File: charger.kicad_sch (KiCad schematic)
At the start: 6 parts, among them U1 BQ24074RGTR

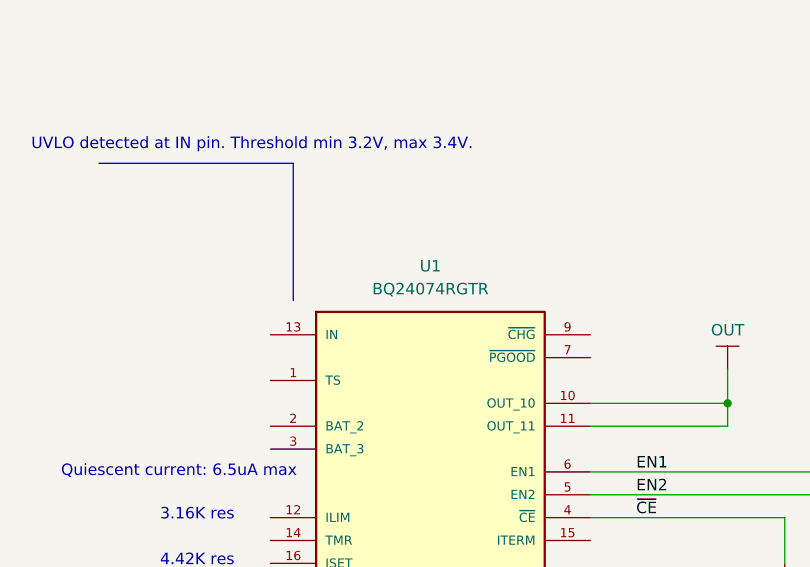
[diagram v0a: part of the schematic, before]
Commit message: Started working on the audio input, including a rough-draft of the first stage.
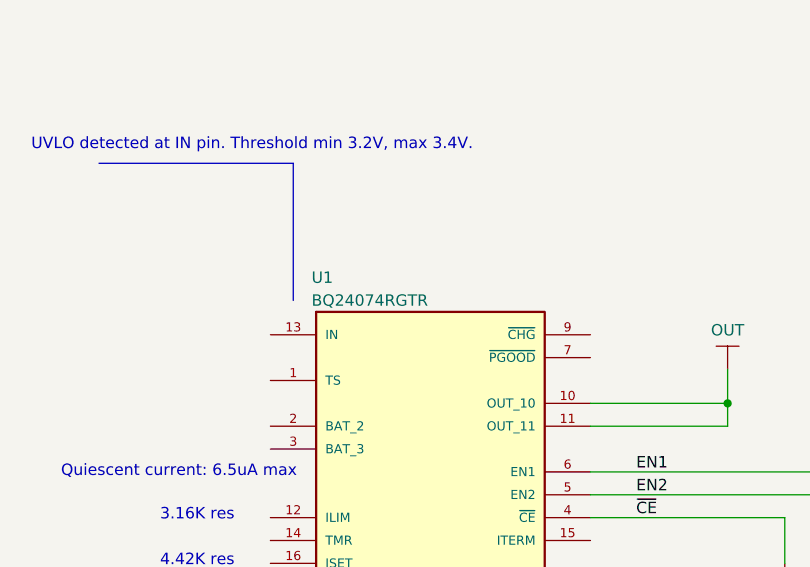
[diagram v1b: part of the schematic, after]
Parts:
- removed U1: BQ24074RGTR, integrated_circuits:bq24074rgtr, symbol integrated_circuits:SINGLE_CELL_LION_CHARGER_BQ24074RGTR
- added U1: BQ24074RGTR, integrated_circuits:bq24074rgtr, symbol #inventree_kicad:BQ24074RGTR
- R1, R2, R3, R4, R5: symbol resistors:R_10K_0402_1PCT_0W0625 -> #inventree_kicad:R_10K_0402_1PCT_0W0625; InvenTree (none) -> 1; MFG Yageo -> (none); PN RC0402FR-0710KL -> (none); Part URL (none) -> http://10.0.0.33/web/part/1/
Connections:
- net EN1: now also U1.6 (EN1)
- net EN2: now also U1.5 (EN2)
- net GND: now also U1.17 (EXP), U1.8 (VSS)
- net OUT: now also U1.10 (OUT_10), U1.11 (OUT_11)
- net ~{CE}: now also U1.4 (~{CE})

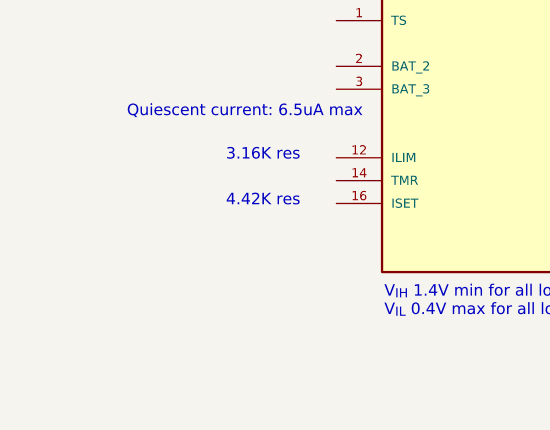
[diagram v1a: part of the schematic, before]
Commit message: Added notes and started work on boost converter.
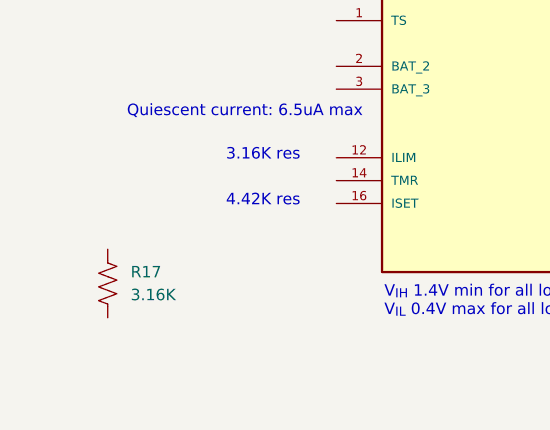
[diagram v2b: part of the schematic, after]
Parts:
- added R17: 3.16K, Resistor_SMD:R_0402_1005Metric, symbol #inventree_kicad:R_3K16_0402_1PCT_0W0625
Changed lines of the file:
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@@
+	)
+	(symbol
+		(lib_id "#inventree_kicad:R_3K16_0402_1PCT_0W0625")
+		(at 73.66 118.11 0)
+		(unit 1)
+		(body_style 1)
+		(exclude_from_sim no)
+		(in_bom yes)
+		(on_board yes)
+		(in_pos_files yes)
+		(dnp no)
+		(fields_autoplaced yes)
+		(property "Reference" "R17"
+			(at 76.2 116.8399 0)
+			(show_name no)
+			(do_not_autoplace no)
+			(effects
+				(font
+					(size 1.27 1.27)
+				)
+				(justify left)
+			)
+		)
+		(property "Value" "3.16K"
+			(at 76.2 119.3799 0)
+			(show_name no)
+			(do_not_autoplace no)
+			(effects
+				(font
+					(size 1.27 1.27)
+				)
+				(justify left)
+			)
+		)
+		(property "Footprint" "Resistor_SMD:R_0402_1005Metric"
+			(at 74.676 118.364 90)
+			(hide yes)
+			(show_name no)
+			(do_not_autoplace no)
+			(effects
+				(font
+					(size 1.27 1.27)
+				)
+			)
+		)
+		(property "Datasheet" ""
+			(at 73.66 118.11 0)
+			(hide yes)
+			(show_name no)
+			(do_not_autoplace no)
+			(effects
+				(font
+					(size 1.27 1.27)
+				)
+			)
+		)
+		(property "Description" "3.16 kOhm ±1% 0.063W, 1/16W Chip Resistor 0402 (1005 Metric)"
+			(at 73.66 118.11 0)
+			(hide yes)
+			(show_name no)
+			(do_not_autoplace no)
+			(effects
+				(font
+					(size 1.27 1.27)
+				)
+			)
+		)
+		(property "IPN" "302-0010"
+			(at 73.66 118.11 0)
+			(hide yes)
+			(show_name no)
+			(do_not_autoplace no)
+			(effects
+				(font
+					(size 1.27 1.27)
+				)
+			)
+		)
+		(property "InvenTree" "27"
+			(at 73.66 118.11 0)
+			(hide yes)
+			(show_name no)
+			(do_not_autoplace no)
+			(effects
+				(font
+					(size 1.27 1.27)
+				)
+			)
+		)
+		(property "Part URL" "http://10.0.0.33/web/part/27/"
+			(at 73.66 118.11 0)
+			(hide yes)
+			(show_name no)
+			(do_not_autoplace no)
+			(effects
+				(font
+					(size 1.27 1.27)
+				)
+			)
+		)
+		(pin "1"
+		)
+		(pin "2"
+		)
+		(instances
+			(project "headphone_amp"
+				(path "/62ffec33-ae93-49a8-bfe6-566578dd8e82/88a6fbe6-41b3-454b-9d65-28a89e2e6ca4"
+					(reference "R17")
+					(unit 1)
+				)
+			)
+		)
 	)
 	(symbol

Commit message: Implemented boost stage and now working on schematics for current buffers and rail splitter.
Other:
- title: (none) -> ${PROJECT_NAME}
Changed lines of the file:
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@@
 	(generator_version "10.0")
 	(paper "A4")
+	(title_block
+		(title "${PROJECT_NAME}")
+		(date "2026-08-25")
+		(rev "${REVISION}")
+		(comment 1 "${PCBA_IPN}")
+	)
 	(text "~{CE} pin: low enables battery charging. Do not leave floating."
 		(exclude_from_sim no)

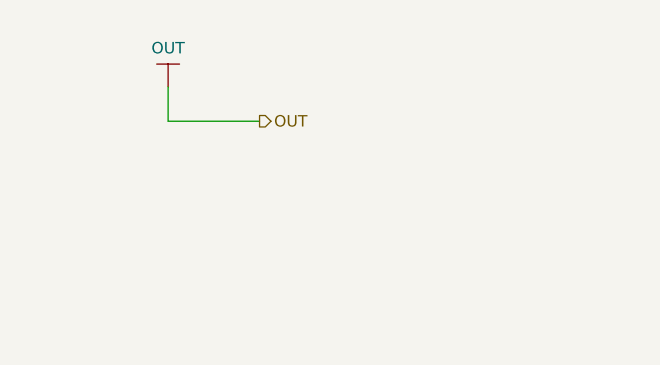
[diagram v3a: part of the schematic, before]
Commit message: Finalizing watchdog and boost circuit.
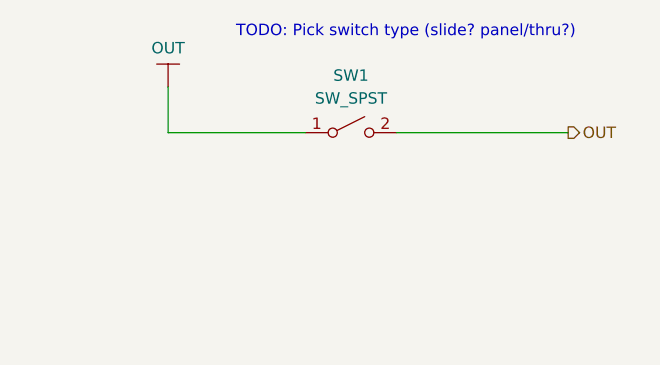
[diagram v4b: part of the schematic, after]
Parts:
- added SW1: SW_SPST, Connector_JST:JST_SH_BM02B-SRSS-TB_1x02-1MP_P1.00mm_Vertical, symbol Switch:SW_SPST
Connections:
- net OUT: now also SW1.1 (A), SW1.2 (B), SW1.MP
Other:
- note added: "TODO: Pick switch type (slide? panel/thru?)"
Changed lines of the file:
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@@
+		)
+	)
+	(text "TODO: Pick switch type (slide? panel/thru?)"
+		(exclude_from_sim no)
+		(at 239.776 21.844 0)
+		(effects
+			(font
+				(size 1.27 1.27)
+			)
 		)
 	)
@@
 	(wire
 		(pts
+			(xy 238.76 33.02) (xy 257.81 33.02)
+		)
+		(stroke
+			(width 0)
+			(type default)
+		)
+	)
+	(wire
+		(pts
 			(xy 184.15 116.84) (xy 184.15 120.65)
 		)
@@
 	(wire
 		(pts
-			(xy 213.36 31.75) (xy 223.52 31.75)
+			(xy 213.36 33.02) (xy 228.6 33.02)
 		)
 		(stroke
@@
 	(wire
 		(pts
-			(xy 213.36 27.94) (xy 213.36 31.75)
+			(xy 213.36 27.94) (xy 213.36 33.02)
 		)
 		(stroke
@@
 	(hierarchical_label "OUT"
 		(shape output)
-		(at 223.52 31.75 0)
+		(at 257.81 33.02 0)
 		(effects
 			(font
@@
 					(unit 1)
 				)
+			)
+		)
+	)
+	(symbol
+		(lib_id "Switch:SW_SPST")
+		(at 233.68 33.02 0)
+		(unit 1)
+		(body_style 1)
+		(exclude_from_sim no)
+		(in_bom yes)
+		(on_board yes)
+		(in_pos_files yes)
+		(dnp no)
+		(fields_autoplaced yes)
+		(property "Reference" "SW1"
+			(at 233.68 26.67 0)
+			(show_name no)
+			(do_not_autoplace no)
+			(effects
+				(font
+					(size 1.27 1.27)
+				)
+			)
+		)
+		(property "Value" "SW_SPST"
+			(at 233.68 29.21 0)
+			(show_name no)
+			(do_not_autoplace no)
+			(effects
+				(font
+					(size 1.27 1.27)
+				)
+			)
+		)
+		(property "Footprint" "Connector_JST:JST_SH_BM02B-SRSS-TB_1x02-1MP_P1.00mm_Vertical"
+			(at 233.68 33.02 0)
+			(hide yes)
+			(show_name no)
+			(do_not_autoplace no)
+			(effects
+				(font
+					(size 1.27 1.27)
+				)
+			)
+		)
+		(property "Datasheet" ""
+			(at 233.68 33.02 0)
+			(hide yes)
+			(show_name no)
+			(do_not_autoplace no)
+			(effects
+				(font
+					(size 1.27 1.27)
+				)
+			)
+		)
+		(property "Description" "Single Pole Single Throw (SPST) switch"
+			(at 233.68 33.02 0)
+			(hide yes)
+			(show_name no)
+			(do_not_autoplace no)
+			(effects
+				(font
+					(size 1.27 1.27)
+				)
+			)
+		)
+		(pin "1"
+		)
+		(pin "2"
+		)
+		(pin "MP"
+		)
+		(pin "MP"
+		)
+		(instances
+			(project "headphone_amp"
+				(path "/62ffec33-ae93-49a8-bfe6-566578dd8e82/88a6fbe6-41b3-454b-9d65-28a89e2e6ca4"
+					(reference "SW1")
+					(unit 1)
+				)

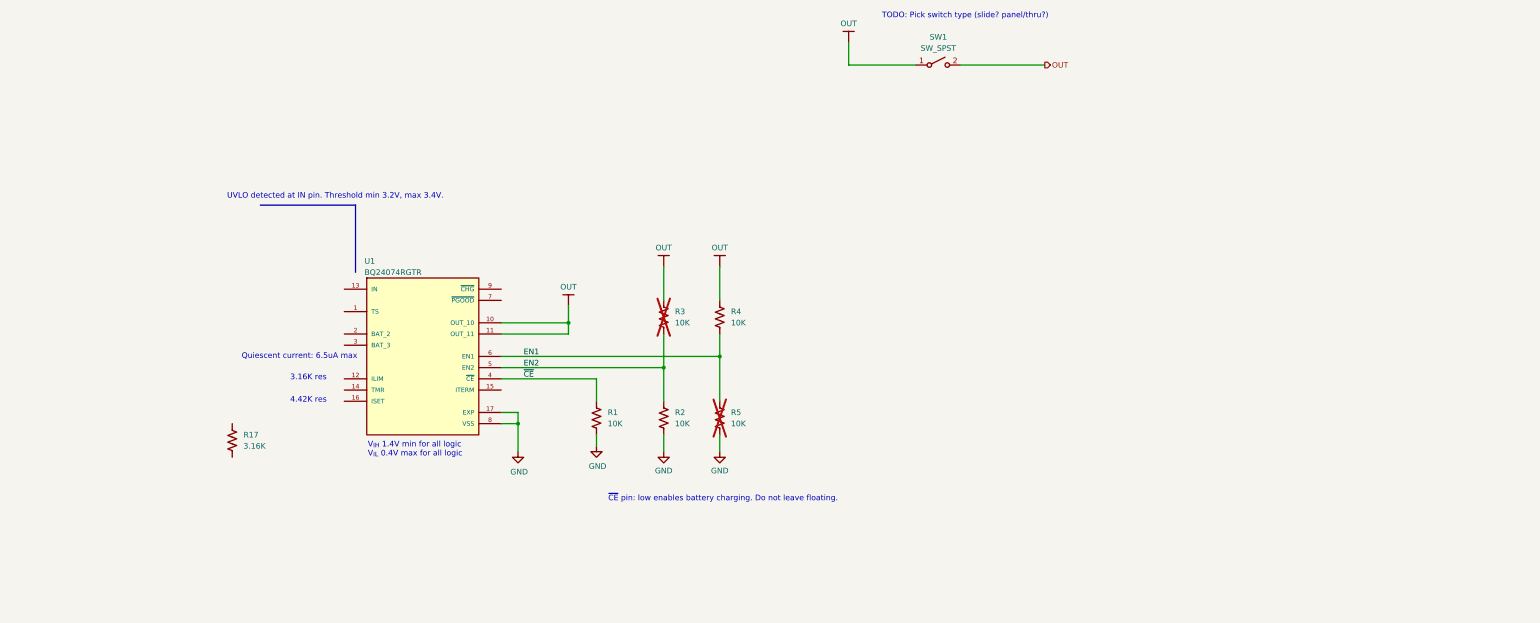
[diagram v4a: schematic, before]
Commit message: First rough draft of schematics complete -- missing a lot of PLM/Inventree work. Ran through several Claude reviews.
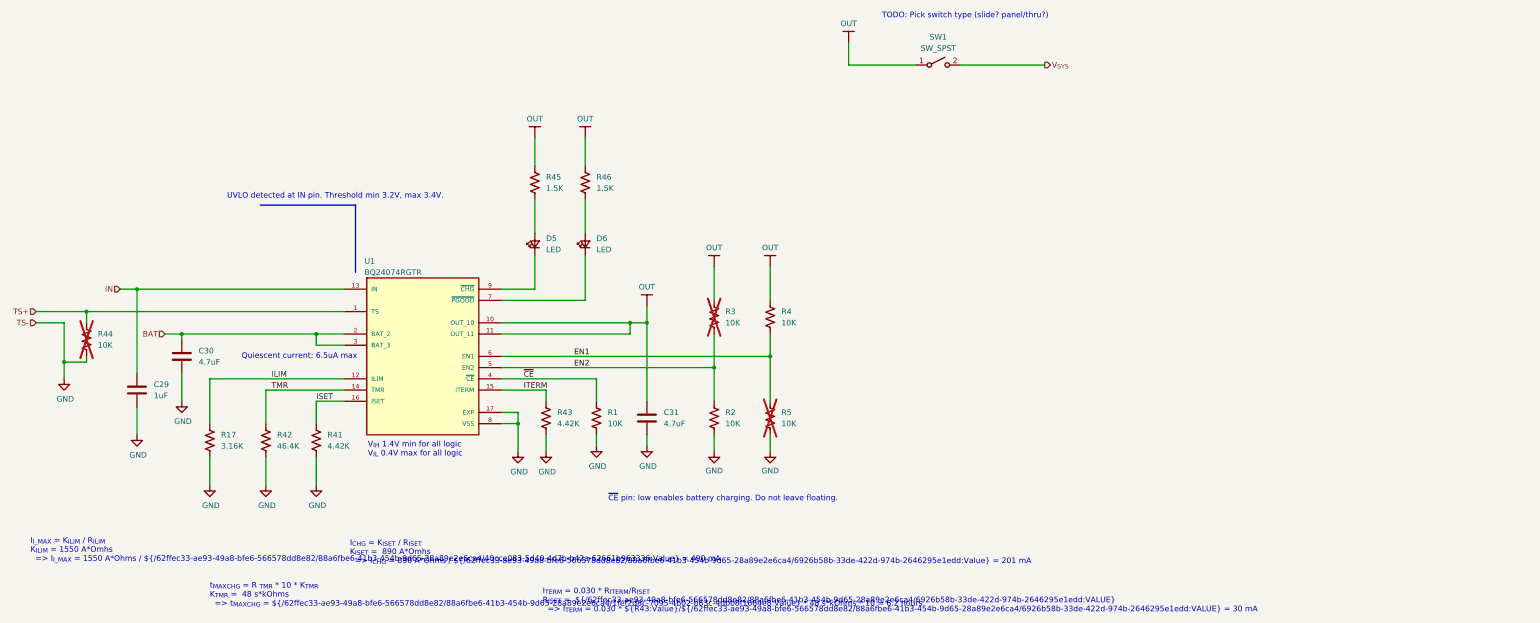
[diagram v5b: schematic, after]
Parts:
- added C29: 1uF, symbol Device:C
- added C30, C31: 4.7uF, symbol Device:C
- added D5, D6: LED, symbol Device:LED_Small
- added R41, R43: 4.42K, symbol Device:R_US
- added R42: 46.4K, symbol Device:R_US
- added R44: 10K, Resistor_SMD:R_0402_1005Metric, symbol #inventree_kicad:R_10K_0402_1PCT_0W0625
- added R45, R46: 1.5K, symbol Device:R_US
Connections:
- net GND: now also R17.2, C29.1, C30.1, C31.1, R41.1, R42.1, R43.1, R44.2
- net OUT: now also C31.2, R45.2, R46.2; no longer SW1.2 (B)
- net TS+: now reaches U1.1 (TS)
- net TS+: now also R44.1
- net ILIM: now reaches U1.12 (ILIM)
- net ILIM: now also R17.1
- net IN: now reaches U1.13 (IN)
- net IN: now also C29.2
- net TMR: now reaches U1.14 (TMR)
- net TMR: now also R42.2
- net ITERM: now reaches U1.15 (ITERM)
- net ITERM: now also R43.2
- net ISET: now reaches U1.16 (ISET)
- net ISET: now also R41.2
- net BAT: now reaches U1.2 (BAT_2)
- net BAT: now also U1.3 (BAT_3), C30.2
- net at U1.7 (~{PGOOD}): now also D6.1 (K)
- net at U1.9 (~{CHG}): now also D5.1 (K)
- new net: D5.2 (A), R45.1
- new net: D6.2 (A), R46.1
- new net V_{SYS}: SW1.2 (B)
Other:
- note added: "I_{CHG} = K_{ISET} / R_{ISET} K_{ISET} = 890 A*Omhs => I_{CHG} = 890 A*Ohms / ${/62ffec33-ae93-49a8-bfe6-566578dd8e82/88a6fbe6-41b3-454b-9d65-28a89e2e6ca4/6926b58b-33de-422d-974b-2646295e1edd:Value} = 201 mA"
- note added: "I_{I_MAX} = K_{ILIM} / R_{ILIM} K_{ILIM} = 1550 A*Omhs => I_{I_MAX} = 1550 A*Ohms / ${/62ffec33-ae93-49a8-bfe6-566578dd8e82/88a6fbe6-41b3-454b-9d65-28a89e2e6ca4/40cce083-5d40-4d7b-b42a-62661b963336:Value} = 490 mA"
- note added: "I_{TERM} = 0.030 * R_{ITERM}/R_{ISET} R_{ISET} = ${/62ffec33-ae93-49a8-bfe6-566578dd8e82/88a6fbe6-41b3-454b-9d65-28a89e2e6ca4/6926b58b-33de-422d-974b-2646295e1edd:VALUE} => I_{TERM} = 0.030 * ${R43:Value}/${/62ffec33-ae93-49a8-bfe6-566578dd8e82/88a6fbe6-41b3-454b-9d65-28a89e2e6ca4/6926b58b-33de-422d-974b-2646295e1edd:VALUE} = 30 mA"
- note added: "t_{MAXCHG} = R _{TMR} * 10 * K_{TMR} K_{TMR} = 48 s*kOhms => t_{MAXCHG} = ${/62ffec33-ae93-49a8-bfe6-566578dd8e82/88a6fbe6-41b3-454b-9d65-28a89e2e6ca4/1fef2d8c-7095-4b02-b63c-4dbb8f1664e8:Value} * 48 s*kOhms * 10 = 6.2 hours"
- note removed: "3.16K res"
- note removed: "4.42K res"
- moved on the sheet: R17, R2, R3, R4, R5

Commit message: Small tunes and adjustments before Inventree work.
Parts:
- D5, D6: value LED -> IN-S42ATA; footprint (none) -> LED_SMD:LED_0402_1005Metric
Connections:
- net ~{PGOOD}: now reaches D6.1 (K), U1.7 (~{PGOOD})
- net ~{CHG}: now reaches D5.1 (K), U1.9 (~{CHG})
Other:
- note added: "Populate R44 if no thermistor on battery"
- moved on the sheet: C29, C30, C31, D5, D6, R1, R17, R2, R3, R4, R41, R42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

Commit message: Started adding new parts to inventree and re-synchronizing here.
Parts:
- R41, R43: footprint (none) -> Resistor_SMD:R_0402_1005Metric; symbol Device:R_US -> #inventree_kicad:R_4K42_0402_1PCT_0W0625; IPN (none) -> 302-0013; InvenTree (none) -> 33; Part URL (none) -> http://10.0.0.33/web/part/33/
- R45, R46: footprint (none) -> Resistor_SMD:R_0402_1005Metric; symbol Device:R_US -> #inventree_kicad:R_1K5_0402_1PCT_0W0625; IPN (none) -> 302-0012; InvenTree (none) -> 32; Part URL (none) -> http://10.0.0.33/web/part/32/
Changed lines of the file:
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@@
 	)
 	(symbol
-		(lib_id "Device:R_US")
+		(lib_id "#inventree_kicad:R_1K5_0402_1PCT_0W0625")
 		(at 153.67 59.69 180)
 		(unit 1)
@@
 			)
 		)
-		(property "Footprint" ""
+		(property "Footprint" "Resistor_SMD:R_0402_1005Metric"
 			(at 152.654 59.436 90)
 			(hide yes)
@@
 			)
 		)
-		(property "Description" "Resistor, US symbol"
+		(property "Description" "1.5 kOhm ±1% 0.063W, 1/16W Chip Resistor 0402 (1005 Metric)"
+			(at 153.67 59.69 0)
+			(hide yes)
+			(show_name no)
+			(do_not_autoplace no)
+			(effects
+				(font
+					(size 1.27 1.27)
+				)
+			)
+		)
+		(property "IPN" "302-0012"
+			(at 153.67 59.69 0)
+			(hide yes)
+			(show_name no)
+			(do_not_autoplace no)
+			(effects
+				(font
+					(size 1.27 1.27)
+				)
+			)
+		)
+		(property "InvenTree" "32"
+			(at 153.67 59.69 0)
+			(hide yes)
+			(show_name no)
+			(do_not_autoplace no)
+			(effects
+				(font
+					(size 1.27 1.27)
+				)
+			)
+		)
+		(property "Part URL" "http://10.0.0.33/web/part/32/"
 			(at 153.67 59.69 0)
 			(hide yes)
@@
 	)
 	(symbol
-		(lib_id "Device:R_US")
+		(lib_id "#inventree_kicad:R_4K42_0402_1PCT_0W0625")
 		(at 104.14 118.11 180)
 		(unit 1)
@@
 			)
 		)
-		(property "Footprint" ""
+		(property "Footprint" "Resistor_SMD:R_0402_1005Metric"
 			(at 103.124 117.856 90)
 			(hide yes)
@@
 			)
 		)
-		(property "Description" "Resistor, US symbol"
+		(property "Description" "4.42 kOhm ±1% 0.063W, 1/16W Chip Resistor 0402 (1005 Metric)"
 			(at 104.14 118.11 0)
 			(hide yes)
@@
 			)
 		)
+		(property "IPN" "302-0013"
+			(at 104.14 118.11 0)
+			(hide yes)
+			(show_name no)
+			(do_not_autoplace no)
+			(effects
+				(font
+					(size 1.27 1.27)
+				)
+			)
+		)
+		(property "InvenTree" "33"
+			(at 104.14 118.11 0)
+			(hide yes)
+			(show_name no)
+			(do_not_autoplace no)
+			(effects
+				(font
+					(size 1.27 1.27)
+				)
+			)
+		)
+		(property "Part URL" "http://10.0.0.33/web/part/33/"
+			(at 104.14 118.11 0)
+			(hide yes)
+			(show_name no)
+			(do_not_autoplace no)
+			(effects
+				(font
+					(size 1.27 1.27)
+				)
+			)
+		)
 		(pin "2"
 		)
@@
 	)
 	(symbol
-		(lib_id "Device:R_US")
+		(lib_id "#inventree_kicad:R_1K5_0402_1PCT_0W0625")
 		(at 170.18 59.69 180)
 		(unit 1)
@@
 			)
 		)
-		(property "Footprint" ""
+		(property "Footprint" "Resistor_SMD:R_0402_1005Metric"
 			(at 169.164 59.436 90)
 			(hide yes)
@@
 			)
 		)
-		(property "Description" "Resistor, US symbol"
+		(property "Description" "1.5 kOhm ±1% 0.063W, 1/16W Chip Resistor 0402 (1005 Metric)"
+			(at 170.18 59.69 0)
+			(hide yes)
+			(show_name no)
+			(do_not_autoplace no)
+			(effects
+				(font
+					(size 1.27 1.27)
+				)
+			)
+		)
+		(property "IPN" "302-0012"
+			(at 170.18 59.69 0)
+			(hide yes)
+			(show_name no)
+			(do_not_autoplace no)
+			(effects
+				(font
+					(size 1.27 1.27)
+				)
+			)
+		)
+		(property "InvenTree" "32"
+			(at 170.18 59.69 0)
+			(hide yes)
+			(show_name no)
+			(do_not_autoplace no)
+			(effects
+				(font
+					(size 1.27 1.27)
+				)
+			)
+		)
+		(property "Part URL" "http://10.0.0.33/web/part/32/"
 			(at 170.18 59.69 0)
 			(hide yes)
@@
 	)
 	(symbol
-		(lib_id "Device:R_US")
+		(lib_id "#inventree_kicad:R_4K42_0402_1PCT_0W0625")
 		(at 156.21 113.03 180)
 		(unit 1)
@@
 			)
 		)
-		(property "Footprint" ""
+		(property "Footprint" "Resistor_SMD:R_0402_1005Metric"
 			(at 155.194 112.776 90)
 			(hide yes)
@@
 			)
 		)
-		(property "Description" "Resistor, US symbol"
+		(property "Description" "4.42 kOhm ±1% 0.063W, 1/16W Chip Resistor 0402 (1005 Metric)"
 			(at 156.21 113.03 0)
 			(hide yes)
+			(show_name no)
+			(do_not_autoplace no)
+			(effects
+				(font
+					(size 1.27 1.27)
+				)
+			)
+		)
+		(property "IPN" "302-0013"
+			(at 156.21 113.03 0)
+			(hide yes)
+			(show_name no)
+			(do_not_autoplace no)
+			(effects
+				(font
+					(size 1.27 1.27)
+				)
+			)
+		)
+		(property "InvenTree" "33"
+			(at 156.21 113.03 0)
+			(hide yes)
+			(show_name no)
+			(do_not_autoplace no)
+			(effects
+				(font
+					(size 1.27 1.27)
+				)
+			)
+		)
+		(property "Part URL" "http://10.0.0.33/web/part/33/"
+			(at 156.21 113.03 0)
+			(hide yes)

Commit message: Updated theory doc, started layout, fixed a footprint.
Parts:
- C29: footprint (none) -> Capacitor_SMD:C_0402_1005Metric
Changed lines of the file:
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@@
 			)
 		)
-		(property "Footprint" ""
+		(property "Footprint" "Capacitor_SMD:C_0402_1005Metric"
 			(at 62.5348 102.87 0)
 			(hide yes)
